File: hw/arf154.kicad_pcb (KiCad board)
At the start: 4 copper layers, 20.3 x 53.3 mm, 21 parts, among them P1 Cn1, P2 Cn2, P3 CONN_02X05, P4 USB_B, U1 ATSAMR21G1x, U2 LD1117S33TR, Y1 16MHz

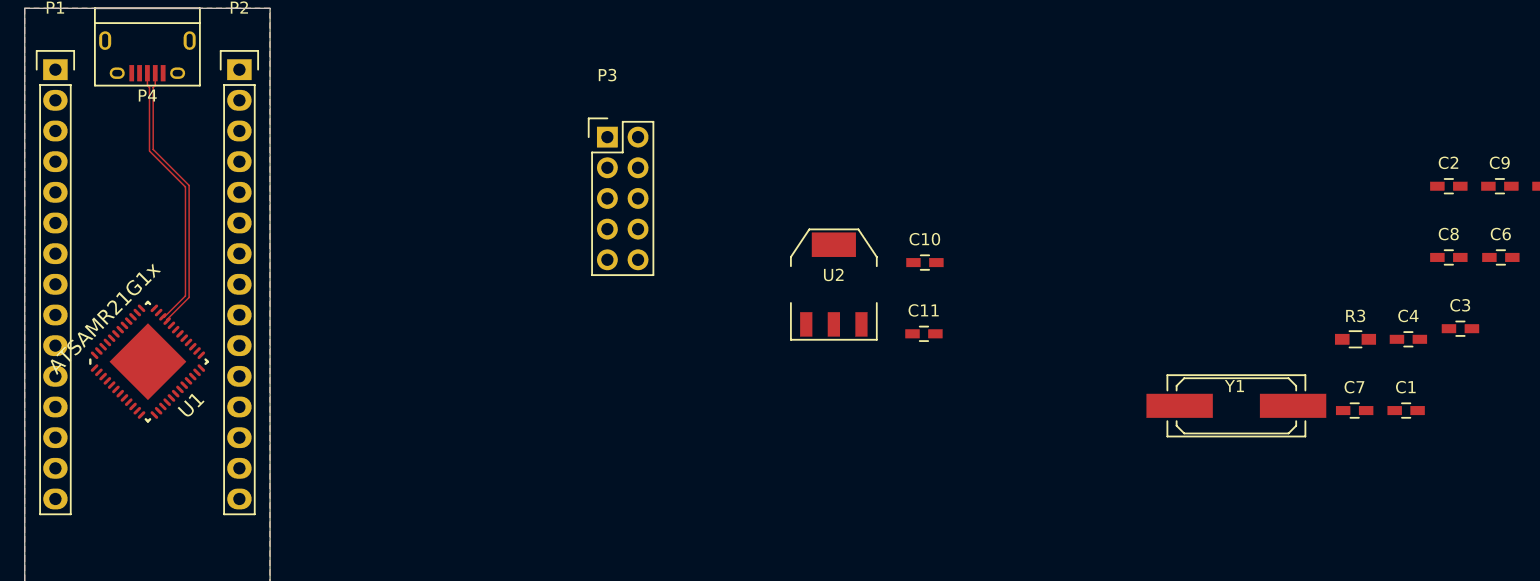
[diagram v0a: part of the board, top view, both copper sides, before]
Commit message: Schematics change for a smaller regulator, added a new sch module, layout update
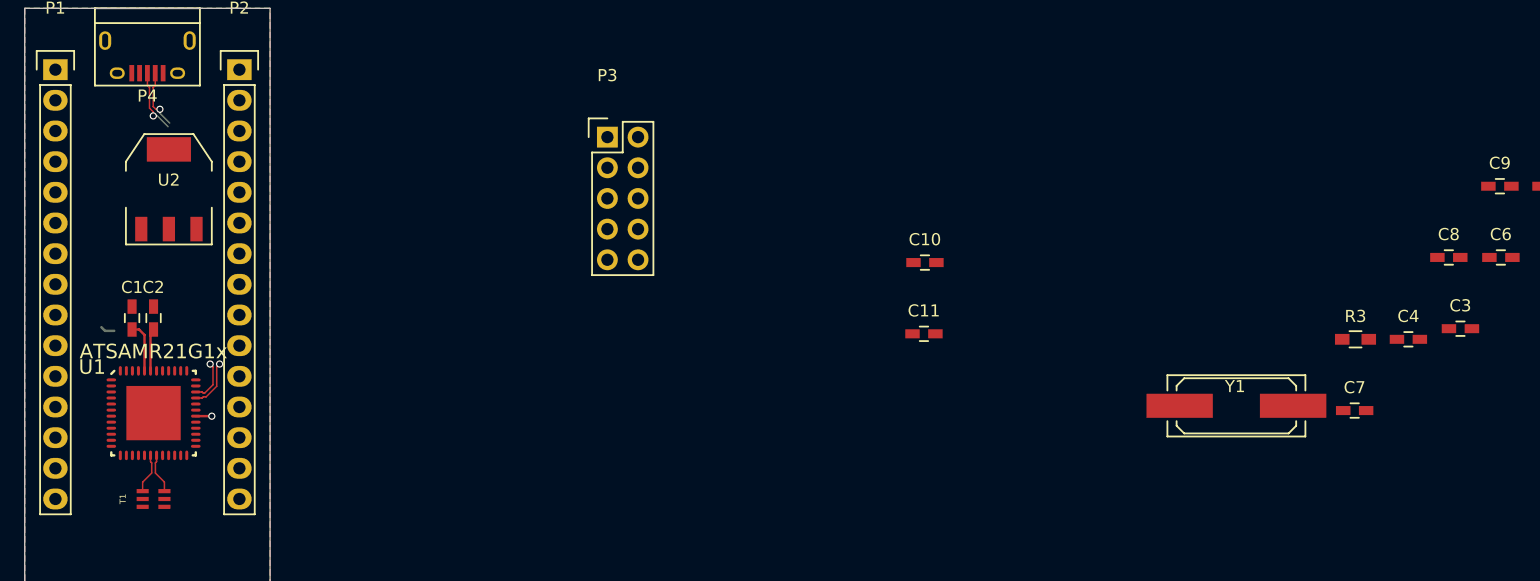
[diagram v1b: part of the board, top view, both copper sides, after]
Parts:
- added T1: 2450BM15A0015, processing:JBALUN, F.Cu at (118.6, 119.4)
- moved C2 107.8 mm to (118.6, 104.4), turned to 90 degrees
- moved C1 105.8 mm to (116.8, 104.4), turned to 90 degrees
- moved U2 55.6 mm to (119.9, 93.7)
- moved U1 4.29 mm to (118.6, 112.3), turned to 0 degrees
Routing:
- net /Sheet557215E3/D+: track 22.6 -> 33.5 mm, vias 0 -> 2
- net /Sheet557215E3/D-: track 22.3 -> 33.1 mm, vias 0 -> 2
- net VDD: track 0.08 -> 9.04 mm, vias 0 -> 1
- net /MainProcessor/BD+: track 0.00 -> 3.31 mm
- net /MainProcessor/BD-: track 0.00 -> 3.31 mm
- net (no net): track 0.00 -> 1.19 mm

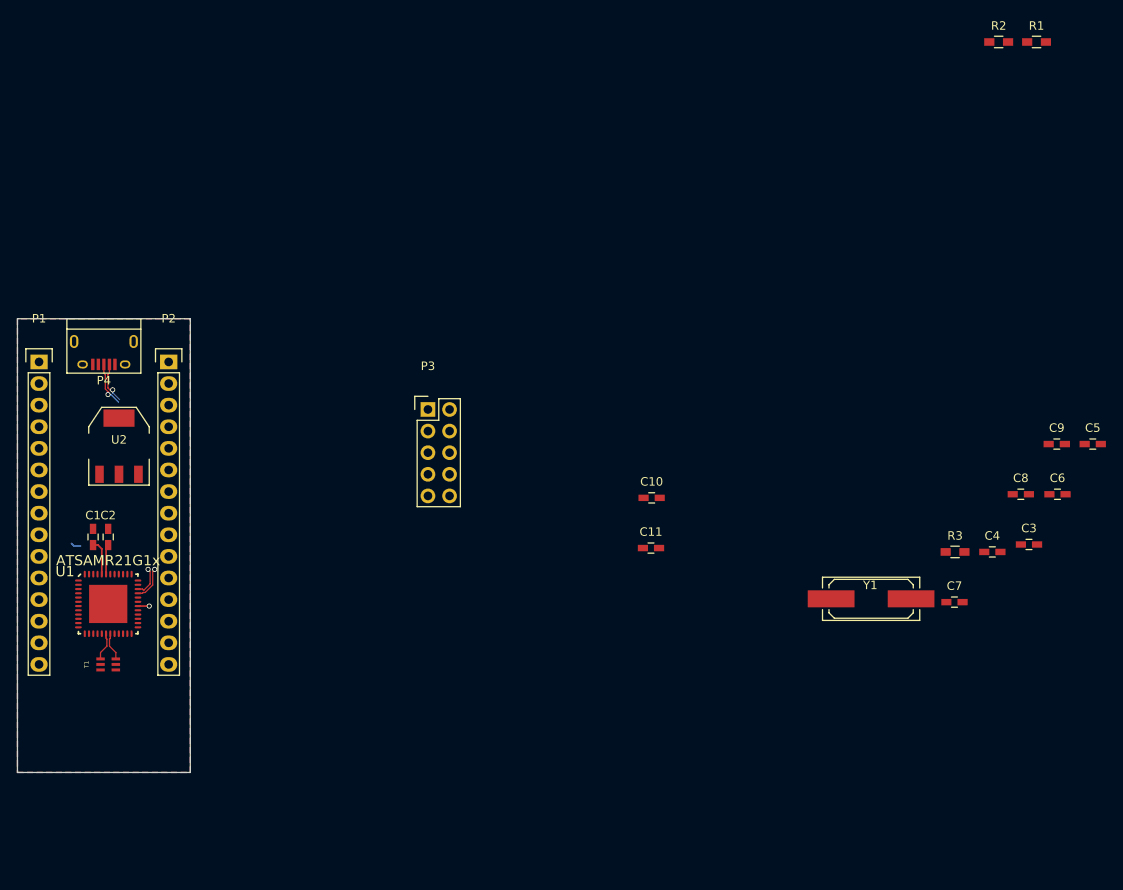
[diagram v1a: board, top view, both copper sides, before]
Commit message: Modified power regulator
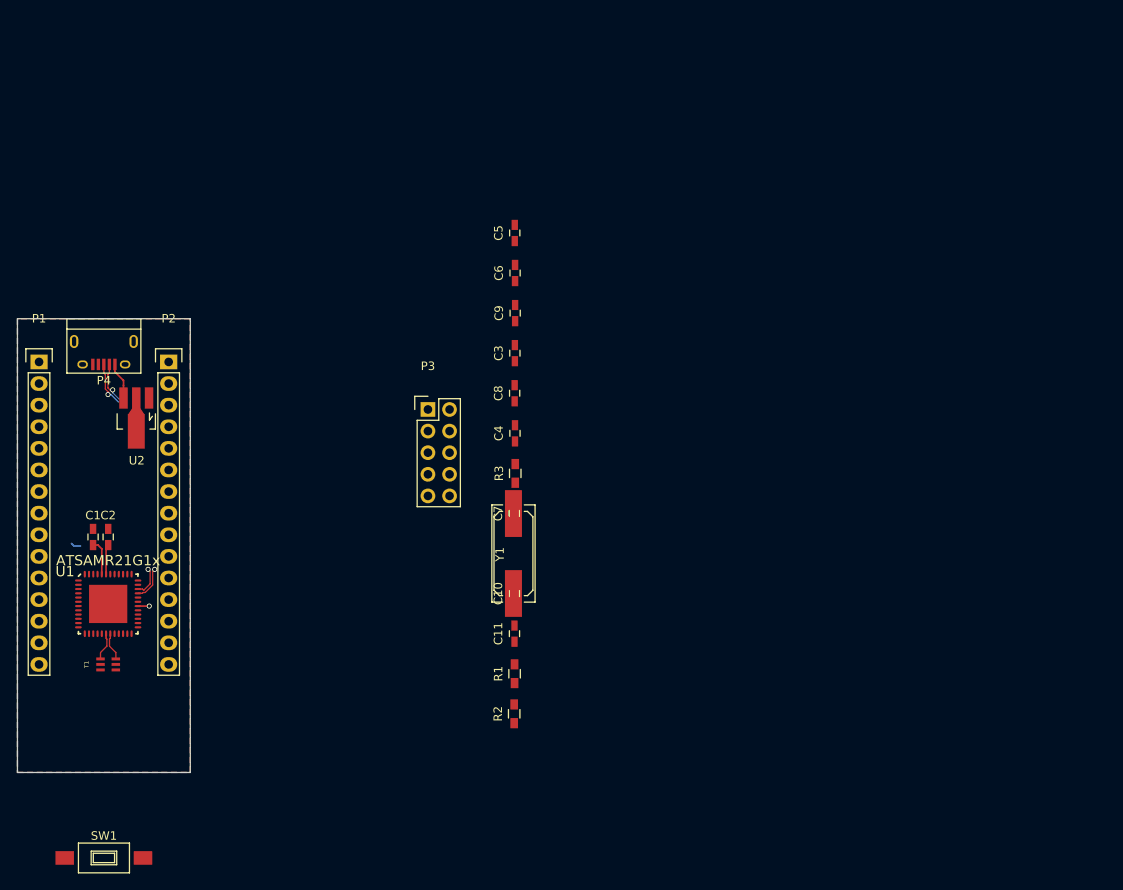
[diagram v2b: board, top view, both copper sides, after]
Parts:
- added SW1: SW_PUSH, Buttons_Switches_SMD:SW_SPST_FSMSM, F.Cu at (118.1, 142.1)
- U2: value LD1117S33TR -> AZ1117C; footprint SOT-223 -> Housings_SOT-89:SOT89-3_Housing_Handsoldering
- moved R2 97.4 mm to (166.3, 125.2), turned to 90 degrees
- moved R1 96.3 mm to (166.4, 120.5), turned to 90 degrees
- moved C5 72.3 mm to (166.4, 68.7), turned to 90 degrees
- moved C6 68.9 mm to (166.4, 73.4), turned to 90 degrees
- moved C9 65.5 mm to (166.5, 78.1), turned to 90 degrees
- moved C3 64.5 mm to (166.4, 82.8), turned to 90 degrees
- moved C8 60.7 mm to (166.4, 87.5), turned to 90 degrees
- moved C4 57.8 mm to (166.4, 92.2), turned to 90 degrees
- moved C7 52.8 mm to (166.4, 101.6), turned to 90 degrees
- moved R3 52.5 mm to (166.5, 96.9), turned to 90 degrees
- moved Y1 42.4 mm to (166.3, 106.3), turned to 90 degrees
- moved C10 19.7 mm to (166.4, 111.1), turned to 90 degrees
- moved C11 18.9 mm to (166.4, 115.8), turned to 90 degrees
- moved U2 3.89 mm to (121.9, 90.4), turned to 180 degrees
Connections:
- P1 pad 1: /TX1 -> (no net)
- P1 pad 10: /D7 -> (no net)
- P1 pad 11: /D8 -> (no net)
- P1 pad 12: /D9 -> (no net)
- P1 pad 13: /D10 -> (no net)
- P1 pad 14: /D11 -> (no net)
- P1 pad 15: /D12 -> (no net)
- P1 pad 2: /RX0 -> (no net)
- P1 pad 5: /D2 -> (no net)
- P1 pad 6: /D3 -> (no net)
- P1 pad 7: /D4 -> (no net)
- P1 pad 8: /D5 -> (no net)
- P1 pad 9: /D6 -> (no net)
- P2 pad 1: /VIN -> (no net)
- P2 pad 10: /A2 -> (no net)
- P2 pad 11: Net-(P2-Pad11) -> (no net)
- P2 pad 12: /A0 -> (no net)
- P2 pad 13: /REF -> (no net)
- P2 pad 15: /D13 -> (no net)
- P2 pad 4: /5V -> (no net)
- P2 pad 5: /A7 -> (no net)
- P2 pad 6: /A6 -> (no net)
- P2 pad 7: /A5 -> (no net)
- P2 pad 8: /A4 -> (no net)
- P2 pad 9: /A3 -> (no net)
- P3 pad 6: Net-(P3-Pad6) -> (no net)
- P3 pad 7: Net-(P3-Pad7) -> (no net)
- P3 pad 8: Net-(P3-Pad8) -> (no net)
- T1 pad 1: Net-(ANT1-Pad~) -> (no net)
- U1 pad 1: /MainProcessor/PA0 -> (no net)
- U1 pad 10: /MainProcessor/PA5 -> (no net)
- U1 pad 11: /MainProcessor/PA6 -> (no net)
- U1 pad 12: /MainProcessor/PA7 -> (no net)
- U1 pad 15: /MainProcessor/PA8 -> (no net)
- U1 pad 16: /MainProcessor/PA9 -> (no net)
- U1 pad 2: /MainProcessor/PA1 -> (no net)
- U1 pad 21: /MainProcessor/PA12 -> (no net)
- U1 pad 22: /MainProcessor/PA13 -> (no net)
- U1 pad 23: /MainProcessor/PA14 -> (no net)
- U1 pad 24: /MainProcessor/PA15 -> (no net)
- U1 pad 25: /MainProcessor/PA16 -> (no net)
- U1 pad 26: /MainProcessor/PA17 -> (no net)
- U1 pad 27: /MainProcessor/PA18 -> (no net)
- U1 pad 28: /MainProcessor/PA19 -> (no net)
- U1 pad 39: /MainProcessor/PA27 -> (no net)
- U1 pad 41: /MainProcessor/PA28 -> (no net)
- U1 pad 47: /MainProcessor/PA2 -> (no net)
- U1 pad 48: /MainProcessor/PA3 -> (no net)
- U1 pad 9: /MainProcessor/PA4 -> (no net)
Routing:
- net VCC: track 0.00 -> 4.36 mm
- net /Sheet557215E3/D-: track 33.1 -> 31.5 mm

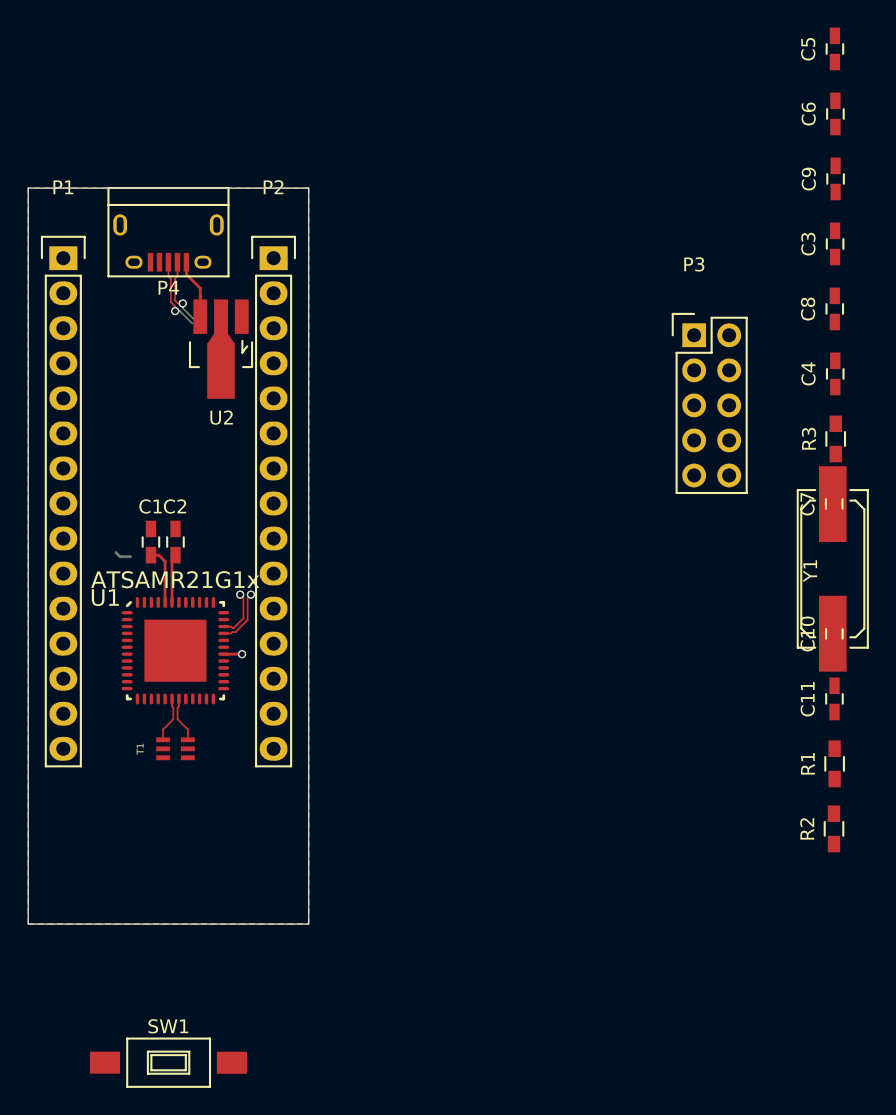
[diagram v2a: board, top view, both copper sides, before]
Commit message: Layout update, footprint changed to 0402, atsam component fix
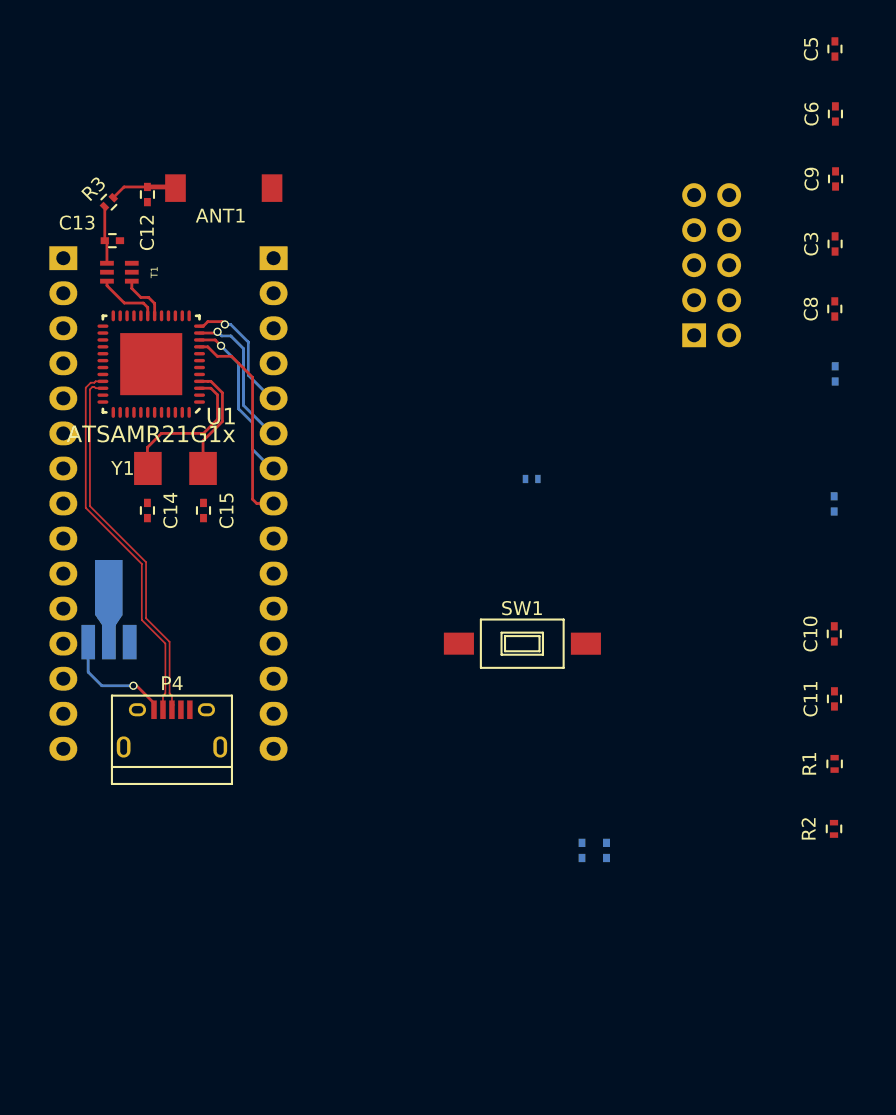
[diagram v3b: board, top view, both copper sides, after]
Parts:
- added ANT1: antenna, processing:CHIPANTENNA2dBi, F.Cu at (118.6, 78.7)
- added C12: xF, Capacitors_SMD:C_0402, F.Cu at (116.6, 79.2)
- added C13: xF, Capacitors_SMD:C_0402, F.Cu at (114.0, 82.5)
- added C14: 18pF, Capacitors_SMD:C_0402, F.Cu at (116.6, 102.1)
- added C15: 18pF, Capacitors_SMD:C_0402, F.Cu at (120.7, 102.1)
- added R4: 10K, Resistors_SMD:R_0402, B.Cu at (144.4, 99.8)
- C1, C2, C4, C7: footprint Capacitors_SMD:C_0603_HandSoldering -> Capacitors_SMD:C_0402; moved to B.Cu
- C10, C11, C3, C5, C6, C8, C9: footprint Capacitors_SMD:C_0603_HandSoldering -> Capacitors_SMD:C_0402
- P1, P2, P3, U2: moved to B.Cu
- R1, R2: footprint Resistors_SMD:R_0603_HandSoldering -> Resistors_SMD:R_0402
- R3: value 10K -> xR; footprint Resistors_SMD:R_0603_HandSoldering -> Resistors_SMD:R_0402
- Y1: footprint Crystals_Oscillators_SMD:Q_49U3HMS -> processing:2SMD
- moved R3 55.4 mm to (113.8, 79.8), turned to 45 degrees
- moved Y1 48.2 mm to (118.6, 99.1), turned to 0 degrees
- moved SW1 39.8 mm to (143.8, 111.8), turned to 180 degrees
- moved C2 38.4 mm to (149.9, 126.7), turned to 270 degrees
- moved C1 38.4 mm to (148.1, 126.7), turned to 270 degrees
- moved P4 35.6 mm to (118.4, 118.1), turned to 0 degrees
- moved T1 34.8 mm to (114.6, 84.8), turned to 90 degrees
- moved U1 20.8 mm to (116.9, 91.5), turned to 180 degrees
- moved U2 20.6 mm to (113.8, 109.3)
- turned C4 to 270 degrees
- turned C7 to 270 degrees
- turned P1 to 180 degrees
- turned P2 to 180 degrees
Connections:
- P1 pad 1: (no net) -> /TX1
- P1 pad 10: (no net) -> /D7
- P1 pad 11: (no net) -> /D8
- P1 pad 12: (no net) -> /D9
- P1 pad 13: (no net) -> /D10
- P1 pad 14: (no net) -> /D11
- P1 pad 15: (no net) -> /D12
- P1 pad 2: (no net) -> /RX0
- P1 pad 5: (no net) -> /D2
- P1 pad 6: (no net) -> /D3
- P1 pad 7: (no net) -> /D4
- P1 pad 8: (no net) -> /D5
- P1 pad 9: (no net) -> /D6
- P2 pad 1: (no net) -> /VIN
- P2 pad 10: (no net) -> /MainProcessor/PA9
- P2 pad 11: (no net) -> /MainProcessor/PB2
- P2 pad 12: (no net) -> /MainProcessor/PB3
- P2 pad 13: (no net) -> /REF
- P2 pad 15: (no net) -> /D13
- P2 pad 4: (no net) -> /5V
- P2 pad 5: (no net) -> /MainProcessor/PA7
- P2 pad 6: (no net) -> /MainProcessor/PA6
- P2 pad 7: (no net) -> /MainProcessor/PA5
- P2 pad 8: (no net) -> /MainProcessor/PA4
- P2 pad 9: (no net) -> /MainProcessor/PA8
- P3 pad 6: (no net) -> Net-(P3-Pad6)
- P3 pad 7: (no net) -> Net-(P3-Pad7)
- P3 pad 8: (no net) -> Net-(P3-Pad8)
- R3 pad 1: VDD -> Net-(C13-Pad1)
- R3 pad 2: /MainProcessor/RST -> Net-(ANT1-Pad1)
- T1 pad 1: (no net) -> Net-(C13-Pad1)
- U1 pad 1: (no net) -> /MainProcessor/PA0
- U1 pad 10: (no net) -> /MainProcessor/PA5
- U1 pad 11: (no net) -> /MainProcessor/PA6
- U1 pad 12: (no net) -> /MainProcessor/PA7
- U1 pad 15: (no net) -> /MainProcessor/PA8
- U1 pad 16: (no net) -> /MainProcessor/PA9
- U1 pad 2: (no net) -> /MainProcessor/PA1
- U1 pad 21: (no net) -> /MainProcessor/PA12
- U1 pad 22: (no net) -> /MainProcessor/PA13
- U1 pad 23: (no net) -> /MainProcessor/PA14
- U1 pad 24: (no net) -> /MainProcessor/PA15
- U1 pad 25: (no net) -> /MainProcessor/PA16
- U1 pad 26: (no net) -> /MainProcessor/PA17
- U1 pad 27: (no net) -> /MainProcessor/PA18
- U1 pad 28: (no net) -> /MainProcessor/PA19
- U1 pad 39: (no net) -> /MainProcessor/PA27
- U1 pad 41: (no net) -> /MainProcessor/PA28
- U1 pad 47: (no net) -> /MainProcessor/PB2
- U1 pad 48: (no net) -> /MainProcessor/PB3
- U1 pad 9: (no net) -> /MainProcessor/PA4
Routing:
- net /MainProcessor/PA4: track 0.00 -> 15.3 mm
- net /MainProcessor/PA5: track 0.00 -> 12.3 mm, vias 0 -> 1
- net /MainProcessor/PA6: track 0.00 -> 10.9 mm, vias 0 -> 1
- net Net-(C14-Pad1): track 0.00 -> 10.7 mm
- net /MainProcessor/PA7: track 0.00 -> 9.22 mm, vias 0 -> 1
- net VDD: track 9.04 -> 0.00 mm, vias 1 -> 0
- net Net-(C15-Pad1): track 0.00 -> 8.11 mm
- net /Sheet557215E3/D+: track 33.5 -> 27.5 mm, vias 2 -> 0
- net Net-(ANT1-Pad1): track 0.00 -> 4.99 mm
- net Net-(C13-Pad1): track 0.00 -> 4.19 mm
- net /Sheet557215E3/D-: track 31.5 -> 27.4 mm, vias 2 -> 0
- net VCC: track 4.36 -> 8.35 mm, vias 0 -> 1
- net /MainProcessor/BD-: track 3.31 -> 4.54 mm
- net (no net): track 1.19 -> 0.34 mm
- removed copper zone on B.Cu, net GND
- removed copper zone on F.Cu, net GND
- removed copper zone on In1.Cu, net GND
- removed copper zone on In2.Cu, net VDD
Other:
- board outline removed
- net class antenna added: clearance 0.1524, trace_width 0.35, via_dia 0.6, via_drill 0.4
